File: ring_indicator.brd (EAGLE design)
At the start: 56.8 x 36.8 mm, 21 parts, among them Q2 BUZ11

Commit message: v0.2-produced
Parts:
- FRITZBOX, INPUT_12V, LICHT1, LICHT2, RUNDUMLEUCHTE: value (none) -> CON_23.81; device pinhead:1X02 -> pcaroli:CON_2_3.81
- R1, R2, R3, R4: device rcl:0204/5 -> rcl:0207/10
- moved C1 10.3 mm to (12.4, 4.45)
- moved R3 8.47 mm to (27.3, 6.99), turned to 180 degrees
- moved R1 5.46 mm to (27.3, 1.91), turned to 0 degrees
- moved R2 4.02 mm to (44.5, 12.7)
- moved R4 3.86 mm to (35.6, 4.45), turned to 180 degrees
- moved LICHT1 3.18 mm to (28.6, 33.0)
- moved LICHT2 3.17 mm to (38.7, 33.0)
- moved C2 3.07 mm to (47.5, 22.9), turned to 0 degrees
- moved Q2 2.84 mm to (54.6, 5.08)
- moved PHONE_IN 2.54 mm to (6.35, 15.2)
- moved FRITZBOX 1.91 mm to (18.4, 33.0)
- moved RUNDUMLEUCHTE 1.90 mm to (48.9, 33.0)
- moved D4 1.27 mm to (26.7, 25.4)
- moved LED1 1.27 mm to (38.1, 25.4)
- moved D2 1.27 mm to (26.7, 14.0)
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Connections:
- net GND: now also FRITZBOX.P$1, INPUT_12V.P$1, LICHT1.P$1, LICHT2.P$1; no longer FRITZBOX.1, INPUT_12V.1, LICHT1.1, LICHT2.1
- net N$6: now also RUNDUMLEUCHTE.P$1; no longer RUNDUMLEUCHTE.1
- net VCC: now also FRITZBOX.P$2, INPUT_12V.P$2, LICHT1.P$2, LICHT2.P$2, RUNDUMLEUCHTE.P$2; no longer FRITZBOX.2, INPUT_12V.2, LICHT1.2, LICHT2.2, RUNDUMLEUCHTE.2
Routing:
- net N$3: track 21.2 -> 11.1 mm
- net N$1: track 11.2 -> 21.0 mm
- net GND: track 139.6 -> 130.2 mm
- net A: track 45.2 -> 37.8 mm
- net N$9: track 19.9 -> 27.3 mm
- net VCC: track 87.2 -> 83.6 mm
- net N$4: track 26.7 -> 23.1 mm
- net B: track 19.8 -> 17.2 mm
- net N$6: track 33.0 -> 31.1 mm
- net N$2: track 6.35 -> 5.08 mm
- net N$10: track 4.50 -> 5.64 mm

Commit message: v0.2.1-cleanup
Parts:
- removed C3: (no value), capacitor-wima:C2.5-3
- removed C5: (no value), resistor:TT2D6
- moved INPUT_12V 4.26 mm to (6.35, 29.2), turned to 270 degrees
- moved R2 1.27 mm to (45.7, 12.7)
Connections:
- net GND: no longer C3.2, C5.-
- net VCC: no longer C3.1, C5.+
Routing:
- net GND: track 130.2 -> 111.0 mm
- net N$6: track 31.1 -> 42.6 mm, vias 2 -> 0
- net VCC: track 83.6 -> 72.7 mm
- net N$9: track 27.3 -> 26.0 mm
- net N$10: track 5.64 -> 5.08 mm
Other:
- board size 56.8 x 36.8 mm -> 53 x 36.8 mm
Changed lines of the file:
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@@
 <?xml version="1.0" encoding="utf-8"?>
 <!DOCTYPE eagle SYSTEM "eagle.dtd">
-<eagle version="7.3.0">
+<eagle version="6.6.0">
 <drawing>
 <settings>
@@
 <board>
 <plain>
-<wire x1="0" y1="0" x2="56.82" y2="0" width="0" layer="20"/>
-<wire x1="56.82" y1="0" x2="56.82" y2="36.82" width="0" layer="20"/>
-<wire x1="56.82" y1="36.82" x2="0" y2="36.82" width="0" layer="20"/>
-<wire x1="0" y1="36.82" x2="0" y2="0" width="0" layer="20"/>
+<wire x1="2.54" y1="0" x2="55.55" y2="0" width="0" layer="20"/>
+<wire x1="55.55" y1="0" x2="55.55" y2="36.82" width="0" layer="20"/>
+<wire x1="55.55" y1="36.82" x2="2.54" y2="36.82" width="0" layer="20"/>
+<wire x1="2.54" y1="36.82" x2="2.54" y2="0" width="0" layer="20"/>
 </plain>
 <attributes>
@@
 <pass name="Default">
 <param name="RoutingGrid" value="50mil"/>
-<param name="AutoGrid" value="1"/>
-<param name="Efforts" value="0"/>
-<param name="TopRouterVariant" value="1"/>
 <param name="tpViaShape" value="round"/>
 <param name="PrefDir.1" value="|"/>
@@
 <element name="LICHT2" library="pcaroli" package="CON_2_3.81" value="CON_23.81" x="38.735" y="33.02" rot="R180"/>
 <element name="RUNDUMLEUCHTE" library="pcaroli" package="CON_2_3.81" value="CON_23.81" x="48.895" y="33.02" rot="R180"/>
-<element name="INPUT_12V" library="pcaroli" package="CON_2_3.81" value="CON_23.81" x="8.255" y="33.02" rot="R180"/>
+<element name="INPUT_12V" library="pcaroli" package="CON_2_3.81" value="CON_23.81" x="6.35" y="29.21" rot="R270"/>
 <element name="C1" library="resistor" package="C102-064X133" value="470n" x="12.446" y="4.445" rot="R180"/>
 <element name="R1" library="rcl" package="0207/10" value="1M" x="27.305" y="1.905"/>
-<element name="R2" library="rcl" package="0207/10" value="1k" x="44.45" y="12.7" rot="R270"/>
+<element name="R2" library="rcl" package="0207/10" value="1k" x="45.72" y="12.7" rot="R270"/>
 <element name="D1" library="diode" package="DO41-10" value="1N4004" x="26.67" y="17.78"/>
 <element name="D2" library="diode" package="DO41-10" value="1N4004" x="26.67" y="13.97" rot="R180"/>
@@
 <element name="Q2" library="transistor-fet" package="TO220" value="BUZ11" x="54.61" y="5.08" rot="R270"/>
 <element name="C2" library="rcl" package="E3,5-8" value="47u" x="47.54965" y="22.86"/>
-<element name="C3" library="capacitor-wima" package="C2.5-3" value="" x="12.7" y="25.4" rot="R270"/>
-<element name="C5" library="resistor" package="TT2D6" value="" x="6.35" y="25.4" rot="R270"/>
 </elements>
 <signals>
@@
 <contactref element="R4" pad="1"/>
 <polygon width="0.6096" layer="16">
-<vertex x="0" y="36.83"/>
-<vertex x="57.15" y="36.83"/>
-<vertex x="57.15" y="0"/>
-<vertex x="0" y="0"/>
+<vertex x="2.54" y="36.83"/>
+<vertex x="55.88" y="36.83"/>
+<vertex x="55.88" y="0"/>
+<vertex x="2.54" y="0"/>
 </polygon>
-<contactref element="INPUT_12V" pad="P$1"/>
-<contactref element="C3" pad="2"/>
-<contactref element="C5" pad="-"/>
-<wire x1="10.795" y1="36.195" x2="5.229903125" y2="36.195" width="0.6096" layer="16"/>
-<wire x1="5.229903125" y1="36.195" x2="3.81" y2="34.775096875" width="0.6096" layer="16"/>
-<wire x1="3.81" y1="34.775096875" x2="3.81" y2="26.67" width="0.6096" layer="16"/>
 <wire x1="20.955" y1="33.02" x2="20.955" y2="36.195" width="1.016" layer="16"/>
 <wire x1="20.955" y1="36.195" x2="10.795" y2="36.195" width="1.016" layer="16"/>
-<wire x1="10.795" y1="36.195" x2="10.795" y2="33.02" width="1.016" layer="16"/>
 <wire x1="31.115" y1="33.02" x2="31.115" y2="36.195" width="1.016" layer="16"/>
 <wire x1="31.115" y1="36.195" x2="20.955" y2="36.195" width="1.016" layer="16"/>
 <wire x1="41.275" y1="33.02" x2="41.275" y2="36.195" width="1.016" layer="16"/>
 <wire x1="41.275" y1="36.195" x2="31.115" y2="36.195" width="1.016" layer="16"/>
-<wire x1="54.61" y1="34.925" x2="53.34" y2="36.195" width="1.016" layer="16"/>
+<wire x1="53.975" y1="35.56" x2="53.34" y2="36.195" width="1.016" layer="16"/>
 <wire x1="53.34" y1="36.195" x2="41.275" y2="36.195" width="1.016" layer="16"/>
-<wire x1="48.26" y1="2.54" x2="54.61" y2="2.54" width="1.016" layer="16"/>
-<wire x1="54.61" y1="2.54" x2="54.61" y2="22.86" width="1.016" layer="16"/>
-<wire x1="54.61" y1="22.86" x2="54.61" y2="34.925" width="1.016" layer="16"/>
-<wire x1="6.35" y1="26.67" x2="3.81" y2="26.67" width="0.6096" layer="16"/>
-<wire x1="12.7" y1="24.13" x2="6.35" y2="24.13" width="0.6096" layer="16"/>
-<wire x1="6.35" y1="24.13" x2="4.708025" y2="24.13" width="0.6096" layer="16"/>
-<wire x1="4.708025" y1="24.13" x2="3.81" y2="25.028025" width="0.6096" layer="16"/>
-<wire x1="3.81" y1="25.028025" x2="3.81" y2="26.67" width="0.6096" layer="16"/>
-<wire x1="54.61" y1="22.86" x2="49.32765" y2="22.86" width="0.6096" layer="16"/>
+<wire x1="48.26" y1="2.54" x2="53.975" y2="2.54" width="1.016" layer="16"/>
+<wire x1="53.975" y1="2.54" x2="53.975" y2="22.86" width="1.016" layer="16"/>
+<wire x1="53.975" y1="22.86" x2="53.975" y2="35.56" width="1.016" layer="16"/>
+<wire x1="53.975" y1="22.86" x2="49.32765" y2="22.86" width="0.6096" layer="16"/>
+<contactref element="INPUT_12V" pad="P$1"/>
+<wire x1="6.35" y1="31.75" x2="10.795" y2="36.195" width="1.016" layer="16"/>
+<wire x1="40.64" y1="4.445" x2="42.545" y2="2.54" width="0.6096" layer="16"/>
+<wire x1="42.545" y1="2.54" x2="48.26" y2="2.54" width="0.6096" layer="16"/>
 </signal>
 <signal name="VCC">
@@
 <wire x1="46.355" y1="30.743025" x2="46.355" y2="33.02" width="1.27" layer="16"/>
 <wire x1="36.83" y1="12.7" x2="36.83" y2="13.820096875" width="0.6096" layer="16"/>
-<wire x1="36.83" y1="13.820096875" x2="38.249903125" y2="15.24" width="0.6096" layer="16"/>
-<wire x1="38.249903125" y1="15.24" x2="41.91" y2="18.900096875" width="0.6096" layer="16"/>
+<wire x1="36.83" y1="13.820096875" x2="41.91" y2="18.900096875" width="0.6096" layer="16"/>
 <wire x1="41.91" y1="18.900096875" x2="41.91" y2="29.845" width="0.6096" layer="16"/>
 <contactref element="INPUT_12V" pad="P$2"/>
-<contactref element="C3" pad="1"/>
-<contactref element="C5" pad="+"/>
-<wire x1="15.875" y1="29.845" x2="12.7" y2="29.845" width="1.27" layer="16"/>
-<wire x1="12.7" y1="29.845" x2="7.72304375" y2="29.845" width="1.27" layer="16"/>
-<wire x1="7.72304375" y1="29.845" x2="5.715" y2="31.85304375" width="1.27" layer="16"/>
-<wire x1="5.715" y1="31.85304375" x2="5.715" y2="33.02" width="1.27" layer="16"/>
-<wire x1="6.35" y1="26.67" x2="12.7" y2="26.67" width="0.6096" layer="16"/>
-<wire x1="12.7" y1="26.67" x2="12.7" y2="29.845" width="0.6096" layer="16"/>
+<wire x1="6.35" y1="26.67" x2="9.525" y2="29.845" width="1.016" layer="16"/>
+<wire x1="9.525" y1="29.845" x2="15.875" y2="29.845" width="1.016" layer="16"/>
 </signal>
 <signal name="A">
@@
 <contactref element="OK1" pad="4"/>
 <contactref element="R2" pad="2"/>
-<wire x1="44.45" y1="7.62" x2="45.72" y2="7.62" width="0.6096" layer="16"/>
 <wire x1="45.72" y1="7.62" x2="48.26" y2="7.62" width="0.6096" layer="16"/>
 <wire x1="30.48" y1="4.445" x2="30.48" y2="7.991975" width="0.6096" layer="16"/>
@@
 <contactref element="Q2" pad="2"/>
 <wire x1="48.26" y1="5.08" x2="51.435" y2="5.08" width="1.016" layer="16"/>
-<wire x1="51.435" y1="5.08" x2="51.435" y2="20.32" width="1.016" layer="16"/>
-<via x="51.435" y="20.32" extent="1-16" drill="1" diameter="1.9304" shape="octagon"/>
-<wire x1="51.435" y1="20.32" x2="51.435" y2="26.035" width="1.016" layer="1"/>
-<via x="51.435" y="26.035" extent="1-16" drill="1" diameter="1.9304" shape="octagon"/>
-<wire x1="51.435" y1="26.035" x2="51.435" y2="33.02" width="1.016" layer="16"/>
+<wire x1="51.435" y1="5.08" x2="51.435" y2="10.16" width="1.016" layer="16"/>
+<wire x1="51.435" y1="10.16" x2="47.625" y2="10.16" width="1.016" layer="16"/>
+<wire x1="47.625" y1="10.16" x2="43.815" y2="13.97" width="1.016" layer="16"/>
+<wire x1="43.815" y1="13.97" x2="43.815" y2="24.765" width="1.016" layer="16"/>
+<wire x1="43.815" y1="24.765" x2="45.72" y2="26.67" width="1.016" layer="16"/>
+<wire x1="45.72" y1="26.67" x2="50.8" y2="26.67" width="1.016" layer="16"/>
+<wire x1="50.8" y1="26.67" x2="51.435" y2="27.305" width="1.016" layer="16"/>
+<wire x1="51.435" y1="27.305" x2="51.435" y2="33.02" width="1.016" layer="16"/>
 </signal>
 <signal name="N$10">
 <contactref element="R2" pad="1"/>
 <contactref element="C2" pad="+"/>
-<wire x1="44.45" y1="17.78" x2="44.45" y2="21.59" width="0.6096" layer="16"/>
-<wire x1="44.45" y1="21.59" x2="45.77165" y2="22.86" width="0.6096" layer="16"/>
+<wire x1="45.72" y1="17.78" x2="45.72" y2="21.59" width="0.6096" layer="16"/>
+<wire x1="45.72" y1="21.59" x2="45.77165" y2="22.86" width="0.6096" layer="16"/>
 </signal>
 </signals>

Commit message: v0.2.2-layout simplified
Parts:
- R4: value 100k -> 50k
- moved Q2 21.9 mm to (48.3, 26.0), turned to 0 degrees
- moved R2 10.9 mm to (44.5, 1.91), turned to 180 degrees
- moved C2 10.8 mm to (48.3, 12.1), turned to 180 degrees
- moved R4 8.98 mm to (44.5, 5.71)
- moved OK1 6.25 mm to (34.3, 10.8)
- moved D1 5.85 mm to (22.2, 14.0)
- moved D2 5.85 mm to (22.2, 10.2)
- moved D3 5.85 mm to (22.2, 17.8)
- moved D4 5.85 mm to (22.2, 21.6)
- moved LED1 5.68 mm to (35.6, 20.3)
- moved R3 5.24 mm to (22.2, 5.71)
- moved C1 5.12 mm to (7.37, 3.81)
- moved R1 5.08 mm to (22.2, 1.91)
- moved RUNDUMLEUCHTE 4.58 mm to (46.4, 29.2)
- moved FRITZBOX 4.58 mm to (15.9, 29.2)
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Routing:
- net N$6: track 42.6 -> 10.2 mm
- net GND: track 111.0 -> 88.6 mm
- net A: track 37.8 -> 29.0 mm
- net N$10: track 5.08 -> 12.2 mm
- net N$9: track 26.0 -> 31.6 mm
- net VCC: track 72.7 -> 76.9 mm
- net B: track 17.2 -> 13.4 mm
- net N$4: track 23.1 -> 26.3 mm
- net N$3: track 11.1 -> 8.26 mm
- net N$5: track 11.4 -> 14.0 mm
- net N$1: track 21.0 -> 18.7 mm
- net N$2: track 5.08 -> 5.71 mm
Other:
- board size 53 x 36.8 mm -> 53 x 33 mm

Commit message: light timing changed
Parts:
- R4: value 50k -> 100k
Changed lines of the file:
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@@
 <element name="R3" library="rcl" package="0207/10" value="2k2" x="22.225" y="5.715" rot="R180"/>
 <element name="LED1" library="led" package="LED5MM" value="" x="35.56" y="20.32"/>
-<element name="R4" library="rcl" package="0207/10" value="50k" x="44.45" y="5.715" rot="R180"/>
+<element name="R4" library="rcl" package="0207/10" value="100k" x="44.45" y="5.715" rot="R180"/>
 <element name="OK1" library="optocoupler" package="DIL06" value="4N27M" x="34.29" y="10.795" rot="R180">
 <attribute name="OC_NEWARK" value="72K9939" x="34.29" y="10.795" size="1.778" layer="27" rot="R180" display="off"/>

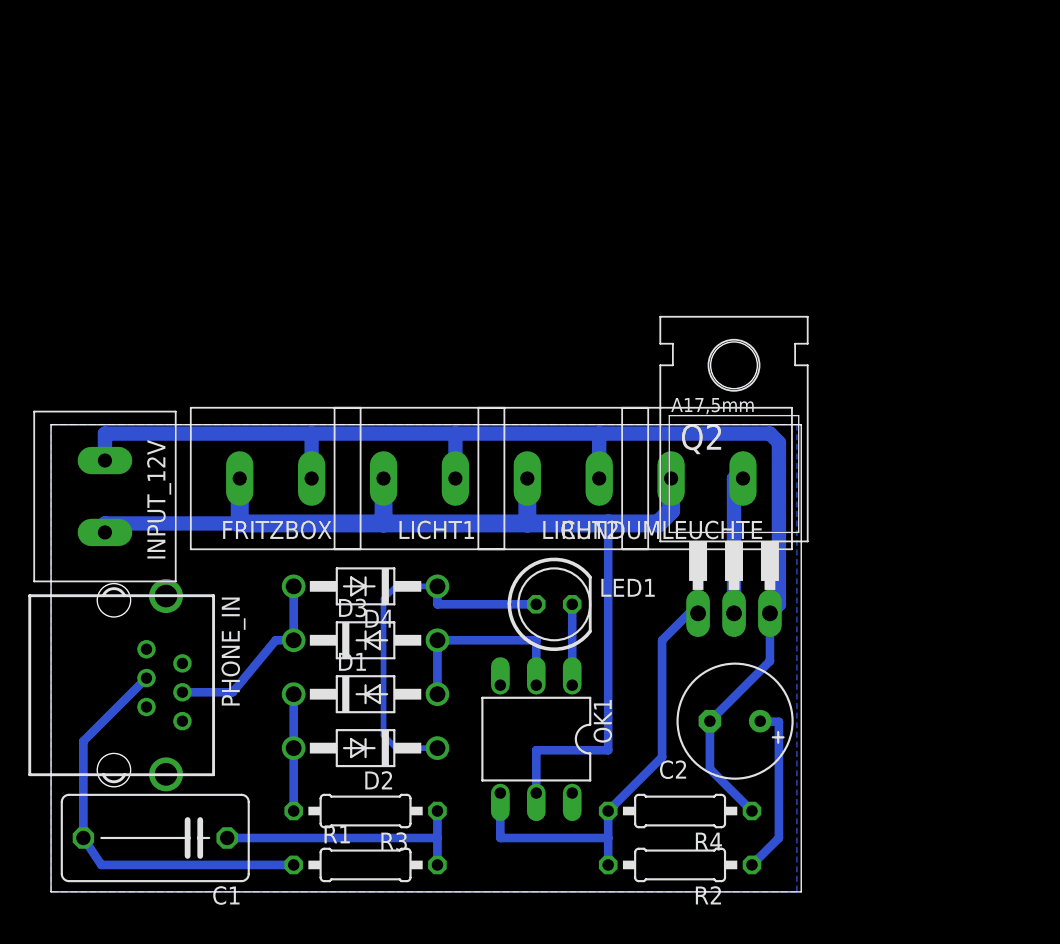
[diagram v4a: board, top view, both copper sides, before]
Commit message: basic poe injector added
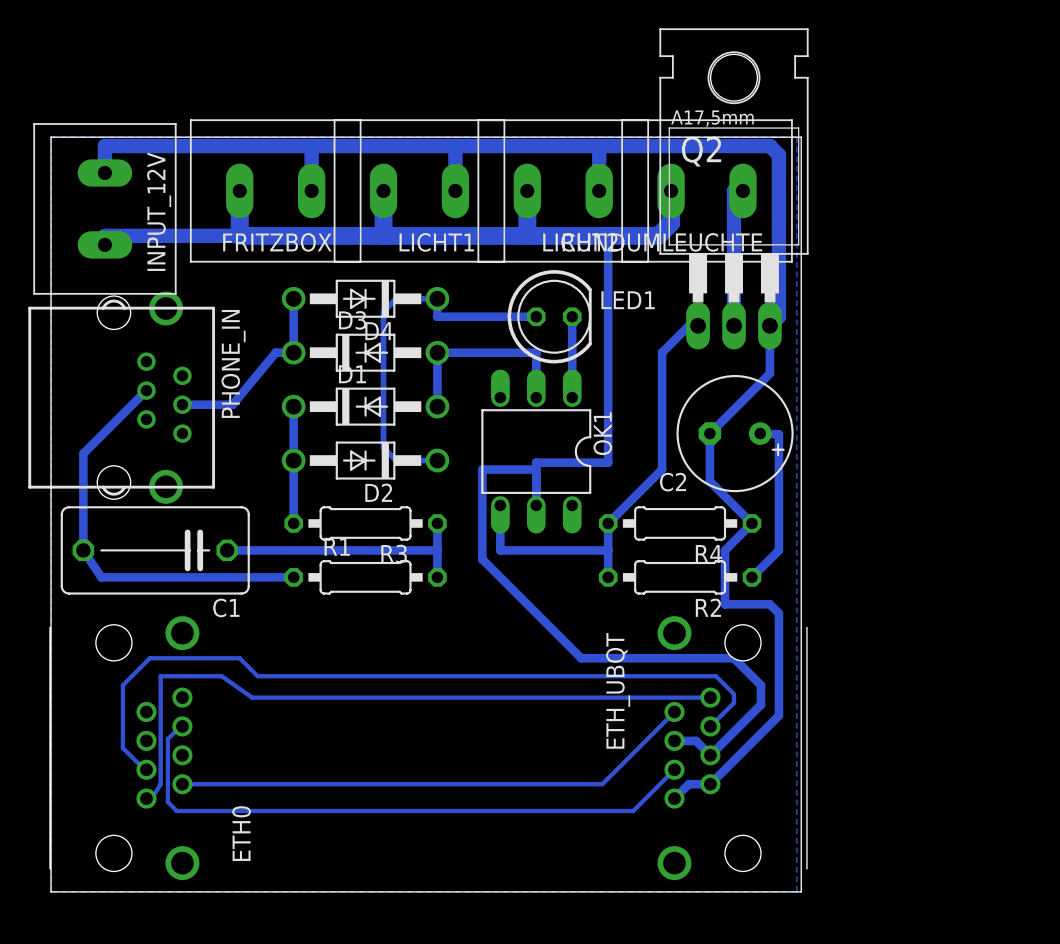
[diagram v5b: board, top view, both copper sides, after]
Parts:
- added ETH0, ETH_UBQT: GLX-S-88M, con-kycon:GLX-S-88M
- moved C1 20.3 mm to (7.37, 24.1)
- moved C2 20.3 mm to (48.3, 32.4)
- moved D1 20.3 mm to (22.2, 34.3)
- moved D2 20.3 mm to (22.2, 30.5)
- moved D3 20.3 mm to (22.2, 38.1)
- moved FRITZBOX 20.3 mm to (15.9, 49.5)
- moved LED1 20.3 mm to (35.6, 40.6)
- moved LICHT1 20.3 mm to (26.0, 49.5)
- moved LICHT2 20.3 mm to (36.2, 49.5)
- moved OK1 20.3 mm to (34.3, 31.1)
- moved R1 20.3 mm to (22.2, 22.2)
- moved R2 20.3 mm to (44.5, 22.2)
- moved R3 20.3 mm to (22.2, 26.0)
- moved R4 20.3 mm to (44.5, 26.0)
- moved RUNDUMLEUCHTE 20.3 mm to (46.4, 49.5)
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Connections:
- new net RX+: ETH0.3, ETH_UBQT.3
- new net RX-: ETH0.6, ETH_UBQT.6
- new net TX+: ETH0.1, ETH_UBQT.1
- new net TX-: ETH0.2, ETH_UBQT.2
- net GND: now also ETH_UBQT.7, ETH_UBQT.8
- net VCC: now also ETH_UBQT.4, ETH_UBQT.5
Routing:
- net RX+: track 0.00 -> 54.7 mm
- net TX+: track 0.00 -> 48.8 mm
- net VCC: track 76.9 -> 122.4 mm
- net RX-: track 0.00 -> 43.1 mm
- net TX-: track 0.00 -> 36.9 mm
- net GND: track 88.6 -> 116.2 mm
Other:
- board size 53 x 33 mm -> 53 x 53.3 mm
